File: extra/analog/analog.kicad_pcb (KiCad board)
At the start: 2 copper layers, 100 x 50 mm, 77 parts, among them J1 Screw_Terminal_01x05, J2 RFShield_OnePiece, J3 Conn_01x05_Pin, J4 Conn_01x04_Socket, J5 Conn_01x04_Socket, J7 Conn_01x04_Socket, U1 THP210, U11 MB85RC04VPNF, U2 INA296A, U3 OPA2196xD, U5 LM27762, U6 ADS1219, U7 REF2033, U8 THP210

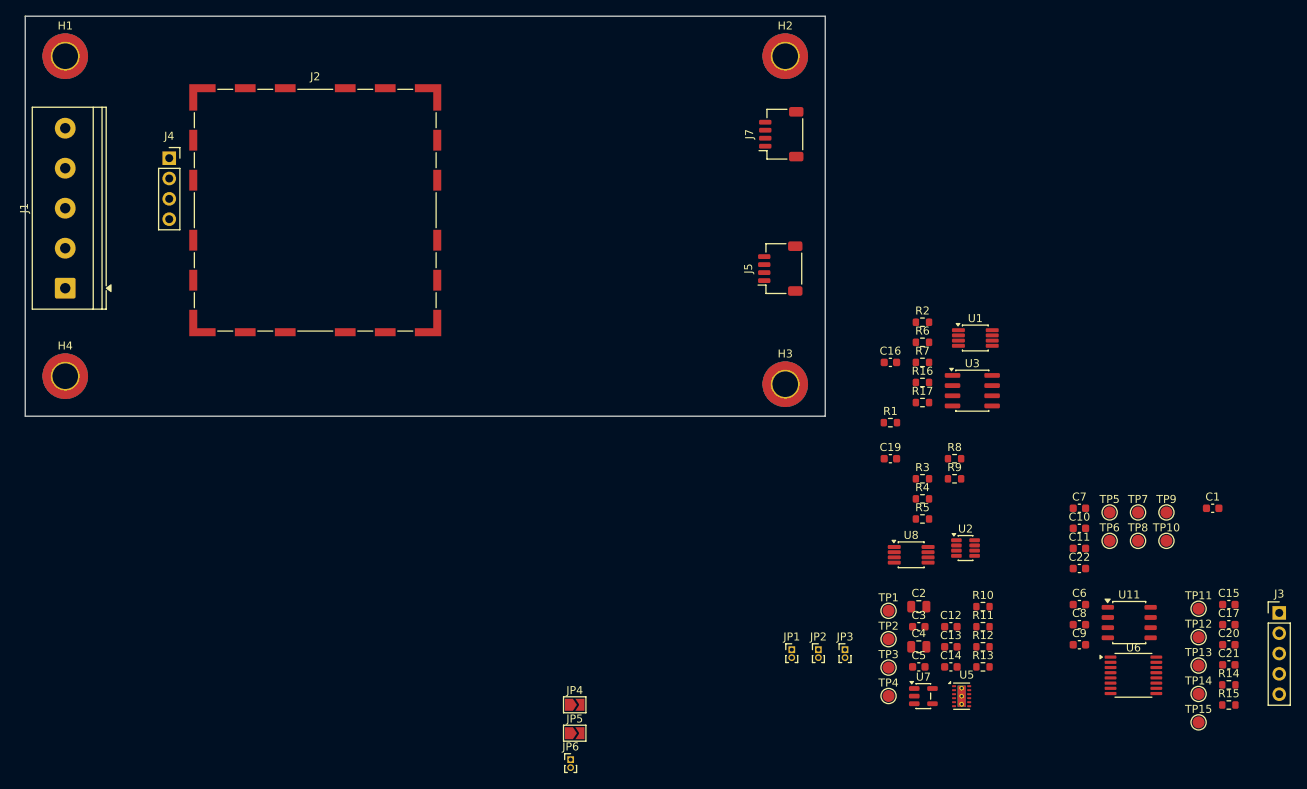
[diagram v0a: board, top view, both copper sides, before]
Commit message: Placed and routed components
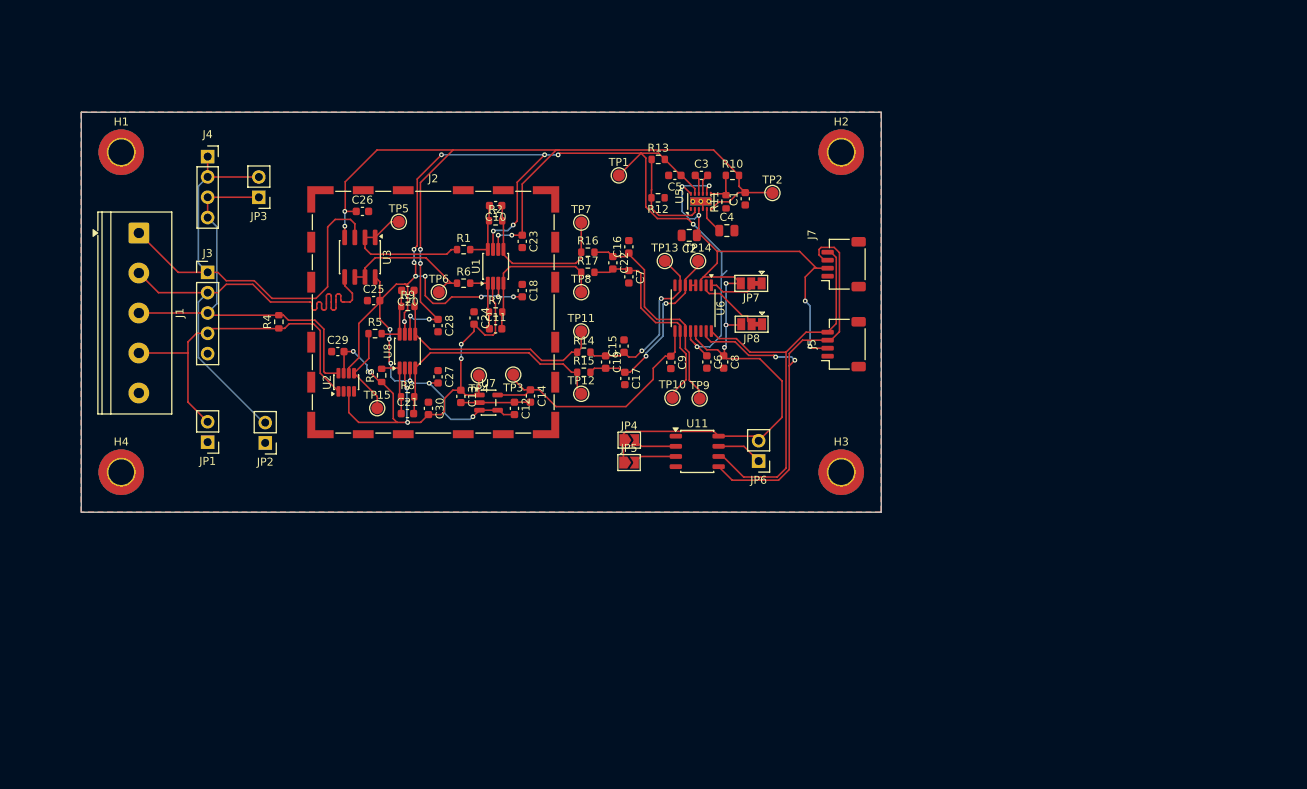
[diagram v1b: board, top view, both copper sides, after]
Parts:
- added C18: 0.1uF, Capacitor_SMD:C_0603_1608Metric, F.Cu at (105.1, 72.3)
- added C23: 0.1uF, Capacitor_SMD:C_0603_1608Metric, F.Cu at (105.1, 66.2)
- added C24: 0.1uF, Capacitor_SMD:C_0603_1608Metric, F.Cu at (99.1, 75.7)
- added C25: 0.1uF, Capacitor_SMD:C_0603_1608Metric, F.Cu at (86.5, 73.5)
- added C26: 0.1uF, Capacitor_SMD:C_0603_1608Metric, F.Cu at (85.2, 62.4)
- added C27: 0.1uF, Capacitor_SMD:C_0603_1608Metric, F.Cu at (94.6, 83.1)
- added C28: 0.1uF, Capacitor_SMD:C_0603_1608Metric, F.Cu at (94.6, 76.7)
- added C29: 0.1uF, Capacitor_SMD:C_0603_1608Metric, F.Cu at (82.1, 79.9)
- added C30: 0.1uF, Capacitor_SMD:C_0603_1608Metric, F.Cu at (93.4, 87.0)
- added JP7: A0, Jumper:SolderJumper-3_P1.3mm_Bridged12_Pad1.0x1.5mm, F.Cu at (133.8, 71.4)
- added JP8: A1, Jumper:SolderJumper-3_P1.3mm_Bridged12_Pad1.0x1.5mm, F.Cu at (133.8, 76.5)
- JP1, JP2, JP3, JP6: footprint Connector_PinHeader_1.00mm:PinHeader_1x02_P1.00mm_Vertical -> Connector_PinHeader_2.54mm:PinHeader_1x02_P2.54mm_Vertical
- TP15: value V_INA -> Ibuf
- moved J3 140.6 mm to (65.8, 70.0)
- moved C20 111.8 mm to (90.8, 72.3), turned to 180 degrees
- moved TP15 109.9 mm to (87.0, 87.0)
- moved C21 107.4 mm to (90.8, 87.7)
- moved TP5 96.0 mm to (89.7, 63.7)
- moved JP3 92.6 mm to (72.2, 60.6), turned to 180 degrees
- moved R14 90.7 mm to (112.8, 80.0)
- moved R15 90.7 mm to (112.8, 82.5)
- moved TP6 89.4 mm to (94.7, 72.5)
- moved TP11 84.6 mm to (112.5, 77.4)
- moved TP13 83.7 mm to (123.0, 68.6)
- moved R4 83.4 mm to (74.7, 76.2), turned to 90 degrees
- moved C10 83.4 mm to (101.8, 61.7), turned to 180 degrees
- moved TP12 82.9 mm to (112.5, 85.2)
- moved TP14 82.7 mm to (127.1, 68.6)
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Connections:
- net Net-(C10-Pad1) renamed /voltage/Vamp+
- net Net-(C11-Pad2) renamed /voltage/Vamp-
- net Net-(C20-Pad1) renamed /current/Iamp+
- net Net-(C21-Pad2) renamed /current/Iamp-
- net Net-(U2-OUT) renamed /current/Ibuf
- net Net-(U3A--) renamed /voltage/Vbuf+
- net Net-(U3B--) renamed /voltage/Vbuf-
- C15 pad 1: /current/OUT_I+ -> /current/Iout+
- C17 pad 1: /current/OUT_I- -> /current/Iout-
- C19 pad 1: /current/OUT_I+ -> /current/Iout+
- C19 pad 2: /current/OUT_I- -> /current/Iout-
- R14 pad 2: /current/OUT_I+ -> /current/Iout+
- R15 pad 2: /current/OUT_I- -> /current/Iout-
- TP13 pad 1: /current/OUT_I+ -> /current/Iout+
- TP14 pad 1: /current/OUT_I- -> /current/Iout-
- U6 pad 1: (no net) -> Net-(JP7-C)
- U6 pad 10: (no net) -> /digital/V-
- U6 pad 11: (no net) -> /digital/V+
- U6 pad 12: (no net) -> +5V
- U6 pad 13: (no net) -> +3V3
- U6 pad 14: (no net) -> unconnected-(U6-~{DRDY}-Pad14)
- U6 pad 15: (no net) -> /digital/SDA
- U6 pad 16: (no net) -> /digital/SCL
- U6 pad 2: (no net) -> Net-(JP8-C)
- U6 pad 3: (no net) -> +3V3
- U6 pad 4: (no net) -> GND
- U6 pad 5: (no net) -> GND
- U6 pad 6: (no net) -> /current/Iout-
- U6 pad 7: (no net) -> /current/Iout+
- U6 pad 8: (no net) -> GND
- U6 pad 9: (no net) -> REF+3V3
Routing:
- net +5V: track 0.00 -> 185.3 mm, vias 0 -> 21
- net -5V: track 0.00 -> 118.8 mm, vias 0 -> 8
- net +3V3: track 0.00 -> 113.1 mm, vias 0 -> 8
- net REF+1V65: track 0.00 -> 65.6 mm, vias 0 -> 6
- net /hardware/IN_V+: track 0.00 -> 62.6 mm
- net /hardware/IN_V-: track 0.00 -> 61.2 mm
- net /digital/SDA: track 0.00 -> 60.8 mm, vias 0 -> 2
- net /hardware/IN_I+: track 0.00 -> 53.0 mm
- net /digital/SCL: track 0.00 -> 52.2 mm
- net /hardware/IN_I-: track 0.00 -> 43.5 mm
- net REF+3V3: track 0.00 -> 32.8 mm
- net /current/Iamp-: track 0.00 -> 30.7 mm
- net /current/Iamp+: track 0.00 -> 30.4 mm
- net /digital/V+: track 0.00 -> 28.2 mm
- net /digital/V-: track 0.00 -> 26.4 mm
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- added copper zone on B.Cu, net GND
- added copper zone on F.Cu, net GND

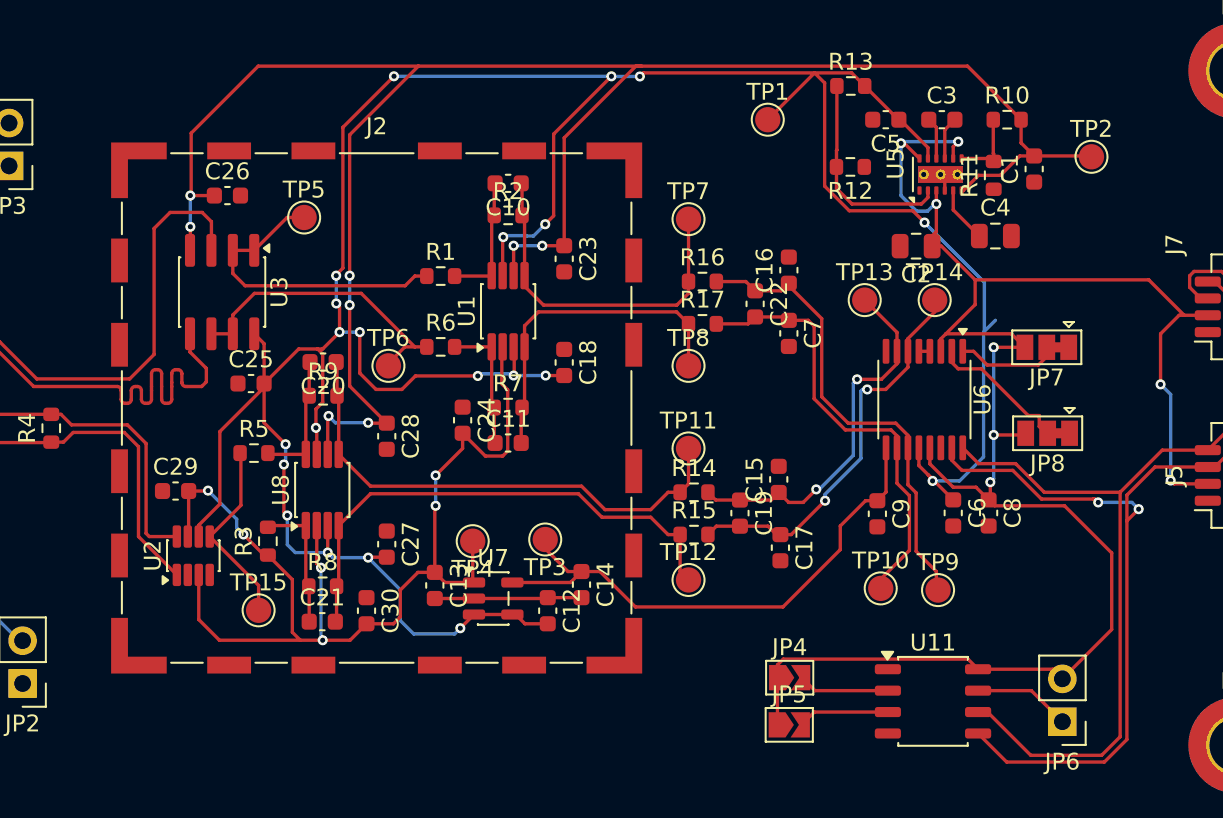
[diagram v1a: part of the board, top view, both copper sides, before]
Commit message: Fixed ERC errors
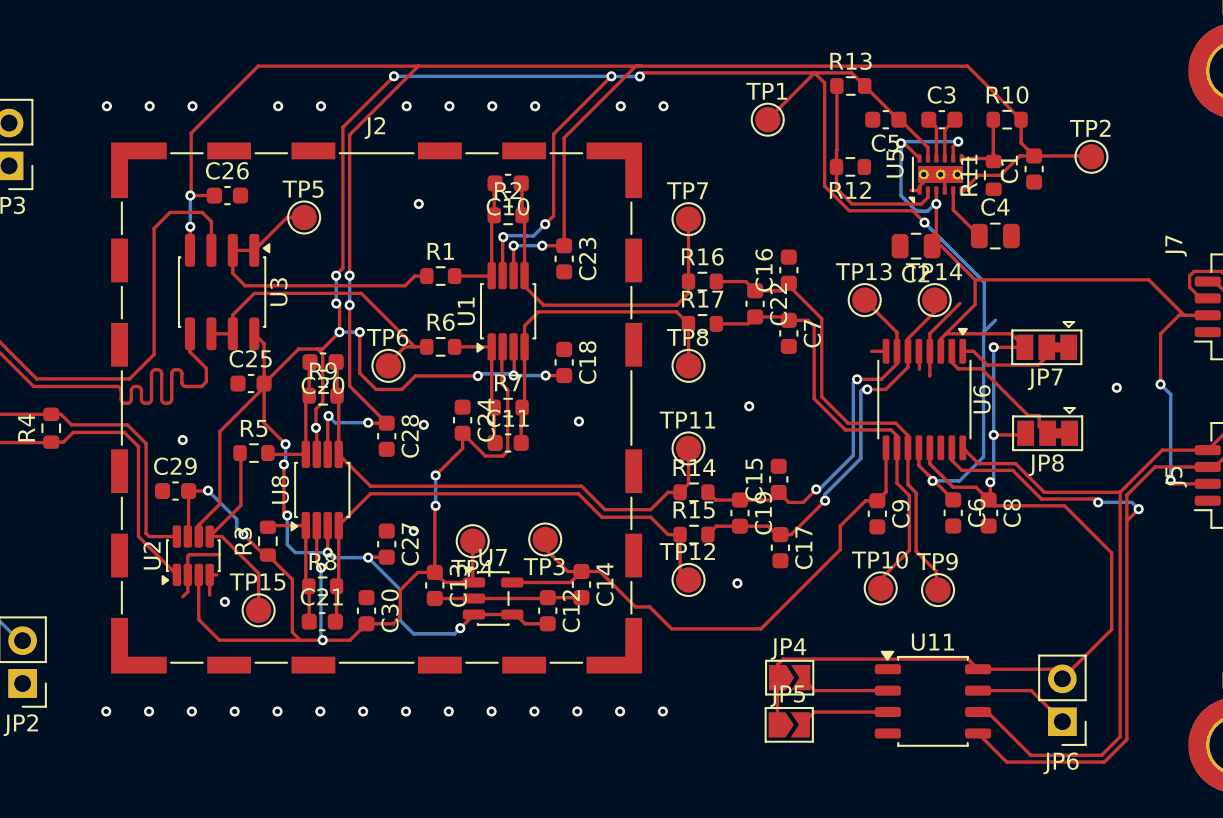
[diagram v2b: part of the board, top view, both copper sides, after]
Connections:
- net /current/Iout+ renamed /current/OUT_I+
- net /current/Iout- renamed /current/OUT_I-
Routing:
- net GND: track 10.4 -> 25.1 mm, vias 0 -> 34
- net REF+3V3: track 32.8 -> 33.9 mm

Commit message: Finalization with jack
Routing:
- net +5V: track 185.3 -> 184.4 mm, vias 21 -> 20
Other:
- board text added: "${TITLE} ${COMPANY} ${REVISION} ${CURRENT_DATE}"
- board text added: "GND"
- board text added: "I+"
- board text added: "I-"
- board text added: "V+"
- board text added: "V-"

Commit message: Hardware fixes
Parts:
- added C31: 47uF, Capacitor_SMD:C_0805_2012Metric, F.Cu at (138.5, 64.2)
- added C34: 10uF, Capacitor_SMD:C_0603_1608Metric, F.Cu at (138.5, 62.2)
- added C37: 47uF, Capacitor_SMD:C_0805_2012Metric, F.Cu at (138.5, 54.6)
- added G***: LOGO, LOGO, F.Cu at (80.1, 54.7)
- added L2: 2.2uH, Inductor_SMD:L_Murata_DFE201610P, F.Cu at (134.3, 58.6)
- added R20: 36.5k, Resistor_SMD:R_0603_1608Metric, F.Cu at (142.6, 60.4)
- added TP16: +3V3, TestPoint:TestPoint_Pad_D1.5mm, F.Cu at (134.4, 63.3)
- added TP17: +5V, TestPoint:TestPoint_Pad_D1.5mm, F.Cu at (134.2, 54.4)
- added U9: TPS63900, Package_SON:WSON-10-1EP_2.5x2.5mm_P0.5mm_EP1.2x2mm_ThermalVias, F.Cu at (138.4, 58.5)
- JP4, JP5: footprint Jumper:SolderJumper-2_P1.3mm_Open_TrianglePad1.0x1.5mm -> Jumper:SolderJumper-2_P1.3mm_Open_RoundedPad1.0x1.5mm
- JP7, JP8: footprint Jumper:SolderJumper-3_P1.3mm_Bridged12_Pad1.0x1.5mm -> Jumper:SolderJumper-3_P1.3mm_Open_RoundedPad1.0x1.5mm
- R10, R12: value 49.9k -> 46.4k
- R11: value 154k -> 130k
- R13: value 158k -> 133k
- R8, R9: value 5k -> 49.9k
- TP1: value +5V -> +4.6V
- TP2: value -5V -> -4.6V
- moved TP2 23.8 mm to (113.8, 52.6)
- moved C1 4.12 mm to (129.6, 58.5)
- moved C2 4.12 mm to (122.6, 63.1)
- moved C3 4.12 mm to (124.1, 55.6)
- moved C5 4.12 mm to (120.8, 55.6)
- moved R13 4.12 mm to (118.7, 53.6)
- moved U5 4.12 mm to (124.0, 58.8)
- moved R11 4.12 mm to (127.2, 58.9), turned to -90 degrees
- moved R12 4.12 mm to (118.7, 58.4)
- moved R10 4.06 mm to (128.2, 55.4), turned to 180 degrees
- moved C4 3.89 mm to (127.3, 62.9)
- moved TP1 3.42 mm to (113.8, 57.5)
- moved R4 1.80 mm to (76.5, 76.2)
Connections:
- C1 pad 2: -5V -> -4.6V
- C12 pad 2: +5V -> +4.6V
- C18 pad 2: +5V -> +4.6V
- C2 pad 1: +3V3 -> +5V
- C23 pad 1: -5V -> -4.6V
- C25 pad 2: +5V -> +4.6V
- C26 pad 1: -5V -> -4.6V
- C27 pad 2: +5V -> +4.6V
- C28 pad 1: -5V -> -4.6V
- C5 pad 1: +5V -> +4.6V
- C6 pad 1: +5V -> +4.6V
- R10 pad 1: Net-(U5-FB-) -> GND
- R10 pad 2: -5V -> Net-(U5-FB-)
- R11 pad 1: GND -> Net-(U5-FB-)
- R11 pad 2: Net-(U5-FB-) -> -4.6V
- R13 pad 2: +5V -> +4.6V
- TP1 pad 1: +5V -> +4.6V
- TP2 pad 1: -5V -> -4.6V
- U1 pad 3: +5V -> +4.6V
- U1 pad 6: -5V -> -4.6V
- U1 pad 7: +5V -> +4.6V
- U2 pad 6: +5V -> +4.6V
- U3 pad 4: -5V -> -4.6V
- U3 pad 8: +5V -> +4.6V
- U5 pad 11: +5V -> +4.6V
- U5 pad 12: +3V3 -> +5V
- U5 pad 3: +3V3 -> +5V
- U5 pad 6: -5V -> -4.6V
- U5 pad 8: +3V3 -> +5V
- U6 pad 12: +5V -> +4.6V
- U7 pad 3: +5V -> +4.6V
- U7 pad 4: +5V -> +4.6V
- U8 pad 3: +5V -> +4.6V
- U8 pad 6: -5V -> -4.6V
- U8 pad 7: +5V -> +4.6V
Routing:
- net +4.6V: track 0.00 -> 185.9 mm, vias 0 -> 20
- net +5V: track 184.4 -> 33.7 mm, vias 20 -> 4
- net -5V: track 118.8 -> 0.00 mm, vias 8 -> 0
- net -4.6V: track 0.00 -> 116.2 mm, vias 0 -> 8
- net Net-(U9-CFG1): track 0.00 -> 4.92 mm
- net Net-(U9-LX1): track 0.00 -> 3.04 mm
- net Net-(U9-LX2): track 0.00 -> 3.03 mm
- net GND: track 25.1 -> 27.8 mm
- net +3V3: track 113.1 -> 110.7 mm, vias 8 -> 5
- net Net-(JP8-C): track 8.47 -> 9.19 mm
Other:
- board text added: "A0"
- board text added: "A1"
- board text added: "A2"
- board text added: "I- to GND"
- board text added: "Load Resi"
- board text added: "One of A1/A2m ust be soldered."
- board text added: "Power J4 -> Load JP1 -> Jumper JP2 -> Jumper"
- board text added: "V+ to I+"
- board text added: "V- to GND"
- board text added: "Voltage J4 -> Empty JP1 -> N/A JP2 -> Jumper"
- board text added: "Write Protect"
- board text added: "±3.3V Voltage ±1mA Current"
